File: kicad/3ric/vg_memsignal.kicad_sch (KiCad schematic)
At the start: 3 parts

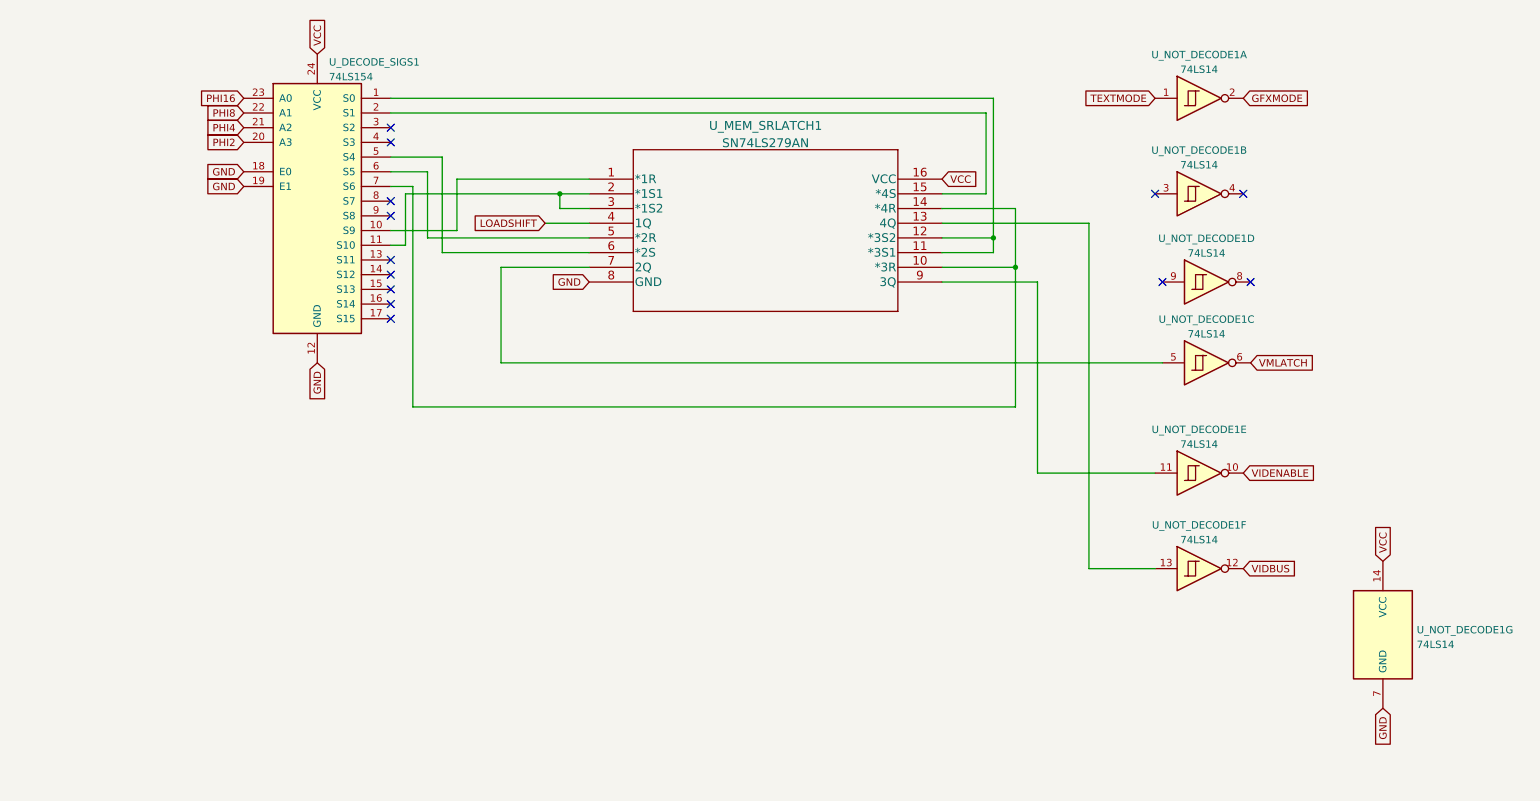
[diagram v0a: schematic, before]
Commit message: schematic updates - bring the schematics up to match breadboard changes current state has high res Apple II color emulation working
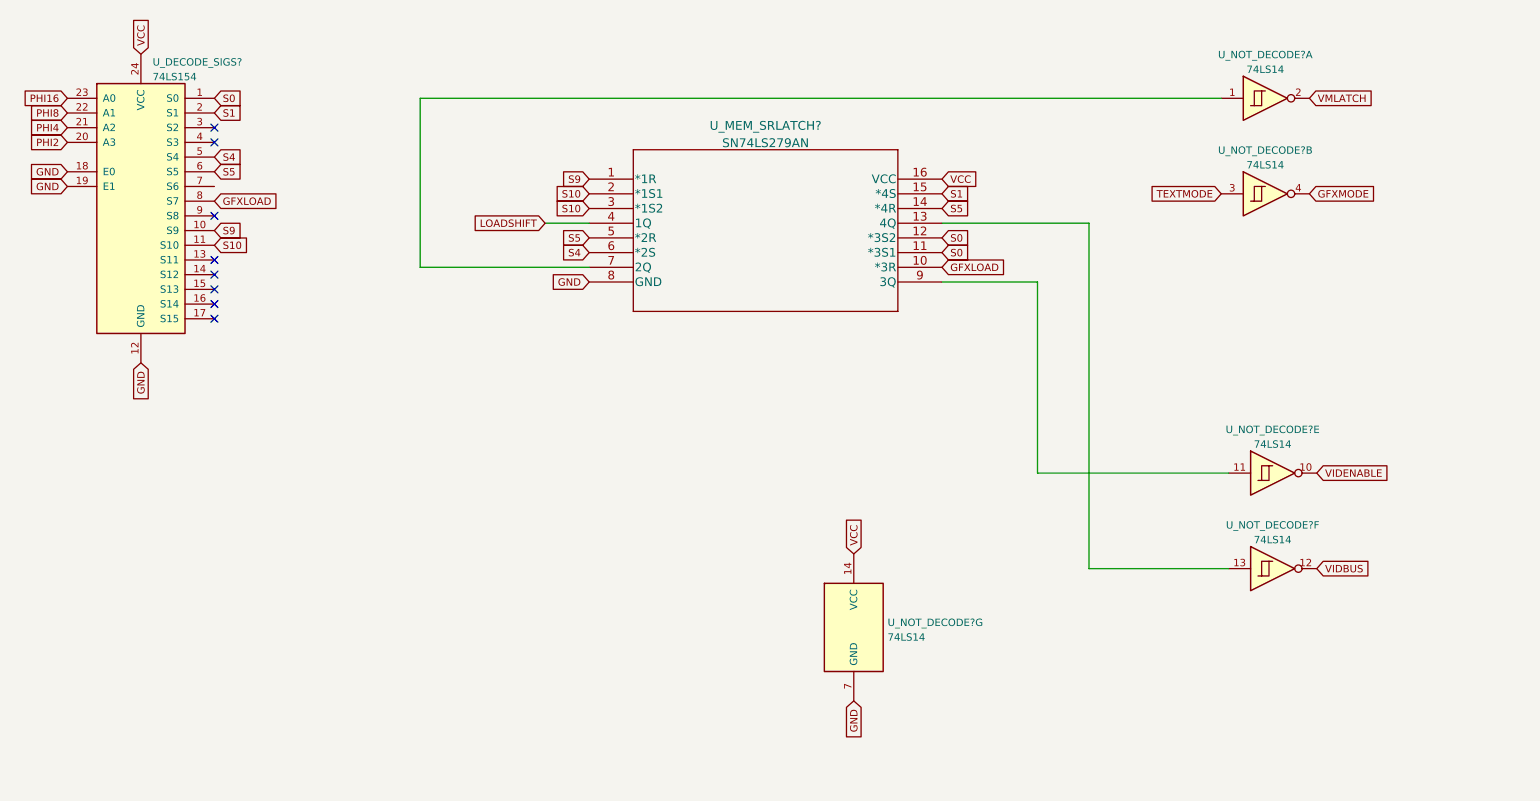
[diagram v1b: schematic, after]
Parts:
- removed unit 4 of U_NOT_DECODE1
- removed unit 3 of U_NOT_DECODE1
- renumbered U_DECODE_SIGS1 to U_DECODE_SIGS?, U_MEM_SRLATCH1 to U_MEM_SRLATCH?, U_NOT_DECODE1 to U_NOT_DECODE?
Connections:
- net GFXMODE: now also U_NOT_DECODE?.4; no longer U_NOT_DECODE?.2
- net TEXTMODE: now also U_NOT_DECODE?.3; no longer U_NOT_DECODE?.1
- net VMLATCH: now also U_NOT_DECODE?.2
- net at U_MEM_SRLATCH?.7 (2Q): now also U_NOT_DECODE?.1
- net S0: now reaches U_DECODE_SIGS?.1 (S0), U_MEM_SRLATCH?.11 (*3S1), U_MEM_SRLATCH?.12 (*3S2)
- net S9: now reaches U_DECODE_SIGS?.10 (S9), U_MEM_SRLATCH?.1 (*1R)
- net S10: now reaches U_DECODE_SIGS?.11 (S10), U_MEM_SRLATCH?.2 (*1S1), U_MEM_SRLATCH?.3 (*1S2)
- net S1: now reaches U_DECODE_SIGS?.2 (S1), U_MEM_SRLATCH?.15 (*4S)
- net S4: now reaches U_DECODE_SIGS?.5 (S4), U_MEM_SRLATCH?.6 (*2S)
- net S5: now reaches U_DECODE_SIGS?.6 (S5), U_MEM_SRLATCH?.5 (*2R)
- net S5: now also U_MEM_SRLATCH?.14 (*4R)
- net GFXLOAD: now reaches U_DECODE_SIGS?.8 (S7)
- net GFXLOAD: now also U_MEM_SRLATCH?.10 (*3R)
- now unconnected: U_DECODE_SIGS?.7 (S6)
- no-connect marks 13 -> 8
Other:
- moved on the sheet: U_DECODE_SIGS?, U_NOT_DECODE?A, U_NOT_DECODE?B, U_NOT_DECODE?E, U_NOT_DECODE?F, U_NOT_DECODE?G

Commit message: updates to logisim project and schematics
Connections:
- net GFXMODE: no longer names the net of U_NOT_DECODE?.4
- net TEXTMODE: no longer names the net of U_NOT_DECODE?.3
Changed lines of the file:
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@@
-    )
-  )
-  (global_label "GFXMODE" (shape input) (at 238.76 60.96 0) (fields_autoplaced)
-    (effects (font (size 1.27 1.27)) (justify left))
-    (property "Intersheet References" "${INTERSHEET_REFS}" (id 0) (at 249.9421 60.8806 0)
-      (effects (font (size 1.27 1.27)) (justify left) hide)
     )
   )
@@
     )
   )
-  (global_label "TEXTMODE" (shape input) (at 223.52 60.96 180) (fields_autoplaced)
-    (effects (font (size 1.27 1.27)) (justify right))
-    (property "Intersheet References" "${INTERSHEET_REFS}" (id 0) (at 211.6121 61.0394 0)
-      (effects (font (size 1.27 1.27)) (justify right) hide)
-    )
-  )

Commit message: push schematic updates
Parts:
- removed U_NOT_DECODE?: 74LS14, Package_DIP:DIP-14_W7.62mm_Socket, symbol 74xx:74LS14
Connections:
- net S9 is gone; now on net GFXLOAD: U_DECODE_SIGS?.10 (S9), U_MEM_SRLATCH?.1 (*1R)
- net GFXLOAD: no longer U_DECODE_SIGS?.8 (S7)
- net S4: no longer U_MEM_SRLATCH?.6 (*2S)
- net S5: no longer U_DECODE_SIGS?.6 (S5), U_MEM_SRLATCH?.5 (*2R)
- net !VIDENABLE: now reaches U_MEM_SRLATCH?.9 (3Q), U_NOT_DECODE?.11
- net at U_NOT_DECODE?.1: no longer U_MEM_SRLATCH?.7 (2Q)
- net VMLATCH: no longer names the net of U_NOT_DECODE?.2
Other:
- note added: "todo: update from breadboard"
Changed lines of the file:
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@@
 (kicad_sch (version 20211123) (generator eeschema)
   (paper "A4")
+  (junction (at 205.74 109.22) (diameter 0) (color 0 0 0 0)
+  )
+  (junction (at 57.15 67.31) (diameter 0) (color 0 0 0 0)
+  )
   (no_connect (at 49.53 82.55))
   (no_connect (at 49.53 52.07))
@@
   (no_connect (at 49.53 49.53))
   (no_connect (at 49.53 64.77))
-  (wire (pts (xy 191.77 109.22) (xy 224.79 109.22))
+  (wire (pts (xy 191.77 109.22) (xy 205.74 109.22))
     (stroke (width 0) (type default) (color 0 0 0 0))
   )
@@
     (stroke (width 0) (type default) (color 0 0 0 0))
   )
+  (wire (pts (xy 57.15 63.5) (xy 57.15 67.31))
+    (stroke (width 0) (type default) (color 0 0 0 0))
+  )
   (wire (pts (xy 200.66 66.04) (xy 200.66 125.73))
     (stroke (width 0) (type default) (color 0 0 0 0))
@@
     (stroke (width 0) (type default) (color 0 0 0 0))
   )
-  (wire (pts (xy 223.52 44.45) (xy 85.09 44.45))
+  (wire (pts (xy 209.55 104.14) (xy 205.74 104.14))
+    (stroke (width 0) (type default) (color 0 0 0 0))
+  )
+  (wire (pts (xy 57.15 67.31) (xy 49.53 67.31))
+    (stroke (width 0) (type default) (color 0 0 0 0))
+  )
+  (wire (pts (xy 205.74 109.22) (xy 224.79 109.22))
     (stroke (width 0) (type default) (color 0 0 0 0))
   )
@@
     (stroke (width 0) (type default) (color 0 0 0 0))
   )
-  (wire (pts (xy 85.09 73.66) (xy 114.3 73.66))
+  (wire (pts (xy 60.96 63.5) (xy 57.15 63.5))
+    (stroke (width 0) (type default) (color 0 0 0 0))
+  )
+  (wire (pts (xy 67.31 67.31) (xy 57.15 67.31))
+    (stroke (width 0) (type default) (color 0 0 0 0))
+  )
+  (wire (pts (xy 205.74 104.14) (xy 205.74 109.22))
     (stroke (width 0) (type default) (color 0 0 0 0))
   )
@@
     (stroke (width 0) (type default) (color 0 0 0 0))
   )
-  (wire (pts (xy 85.09 44.45) (xy 85.09 73.66))
-    (stroke (width 0) (type default) (color 0 0 0 0))
-  )
   (wire (pts (xy 191.77 76.2) (xy 191.77 109.22))
     (stroke (width 0) (type default) (color 0 0 0 0))
   )
+  (text "todo: update from breadboard\n" (at 67.31 90.17 0)
+    (effects (font (size 1.27 1.27)) (justify left bottom))
+  )
   (global_label "S4" (shape input) (at 49.53 54.61 0) (fields_autoplaced)
     (effects (font (size 1.27 1.27)) (justify left))
@@
     )
   )
-  (global_label "VMLATCH" (shape input) (at 238.76 44.45 0) (fields_autoplaced)
-    (effects (font (size 1.27 1.27)) (justify left))
-    (property "Intersheet References" "${INTERSHEET_REFS}" (id 0) (at 249.3979 44.3706 0)
-      (effects (font (size 1.27 1.27)) (justify left) hide)
-    )
-  )
   (global_label "PHI4" (shape input) (at 24.13 49.53 180) (fields_autoplaced)
     (effects (font (size 1.27 1.27)) (justify right))
@@
     )
   )
-  (global_label "GND" (shape input) (at 160.02 148.59 270) (fields_autoplaced)
-    (effects (font (size 1.27 1.27)) (justify right))
-    (property "Intersheet References" "${INTERSHEET_REFS}" (id 0) (at 159.9406 154.8736 90)
-      (effects (font (size 1.27 1.27)) (justify right) hide)
-    )
-  )
-  (global_label "VCC" (shape input) (at 160.02 123.19 90) (fields_autoplaced)
-    (effects (font (size 1.27 1.27)) (justify left))
-    (property "Intersheet References" "${INTERSHEET_REFS}" (id 0) (at 159.9406 117.1483 90)
-      (effects (font (size 1.27 1.27)) (justify left) hide)
-    )
-  )
   (global_label "S0" (shape input) (at 175.26 71.12 0) (fields_autoplaced)
     (effects (font (size 1.27 1.27)) (justify left))
@@
     )
   )
-  (global_label "S4" (shape input) (at 114.3 71.12 180) (fields_autoplaced)
-    (effects (font (size 1.27 1.27)) (justify right))
-    (property "Intersheet References" "${INTERSHEET_REFS}" (id 0) (at 109.4679 71.1994 0)
-      (effects (font (size 1.27 1.27)) (justify right) hide)
-    )
-  )
   (global_label "S0" (shape input) (at 49.53 44.45 0) (fields_autoplaced)
     (effects (font (size 1.27 1.27)) (justify left))
@@
     )
   )
+  (global_label "!VIDENABLE" (shape input) (at 209.55 104.14 0) (fields_autoplaced)
+    (effects (font (size 1.27 1.27)) (justify left))
+    (property "Intersheet References" "${INTERSHEET_REFS}" (id 0) (at 222.5464 104.0606 0)
+      (effects (font (size 1.27 1.27)) (justify left) hide)
+    )
+  )
   (global_label "GFXLOAD" (shape input) (at 175.26 73.66 0) (fields_autoplaced)
     (effects (font (size 1.27 1.27)) (justify left))
@@
     )
   )
-  (global_label "S5" (shape input) (at 49.53 57.15 0) (fields_autoplaced)
-    (effects (font (size 1.27 1.27)) (justify left))
-    (property "Intersheet References" "${INTERSHEET_REFS}" (id 0) (at 54.3621 57.0706 0)
-      (effects (font (size 1.27 1.27)) (justify left) hide)
-    )
-  )
   (global_label "S5" (shape input) (at 175.26 63.5 0) (fields_autoplaced)
     (effects (font (size 1.27 1.27)) (justify left))
@@
     )
   )
-  (global_label "S9" (shape input) (at 49.53 67.31 0) (fields_autoplaced)
-    (effects (font (size 1.27 1.27)) (justify left))
-    (property "Intersheet References" "${INTERSHEET_REFS}" (id 0) (at 54.3621 67.2306 0)
-      (effects (font (size 1.27 1.27)) (justify left) hide)
-    )
-  )
-  (global_label "GFXLOAD" (shape input) (at 49.53 62.23 0) (fields_autoplaced)
-    (effects (font (size 1.27 1.27)) (justify left))
-    (property "Intersheet References" "${INTERSHEET_REFS}" (id 0) (at 60.2283 62.1506 0)
+  (global_label "S9" (shape input) (at 67.31 67.31 0) (fields_autoplaced)
+    (effects (font (size 1.27 1.27)) (justify left))
+    (property "Intersheet References" "${INTERSHEET_REFS}" (id 0) (at 72.1421 67.2306 0)
       (effects (font (size 1.27 1.27)) (justify left) hide)
     )
@@
     )
   )
-  (global_label "S5" (shape input) (at 114.3 68.58 180) (fields_autoplaced)
-    (effects (font (size 1.27 1.27)) (justify right))
-    (property "Intersheet References" "${INTERSHEET_REFS}" (id 0) (at 109.4679 68.6594 0)
-      (effects (font (size 1.27 1.27)) (justify right) hide)
-    )
-  )
   (global_label "PHI2" (shape input) (at 24.13 52.07 180) (fields_autoplaced)
     (effects (font (size 1.27 1.27)) (justify right))
@@
     (property "Intersheet References" "${INTERSHEET_REFS}" (id 0) (at 17.8464 57.0706 0)
       (effects (font (size 1.27 1.27)) (justify right) hide)
+    )
+  )
+  (global_label "GFXLOAD" (shape input) (at 60.96 63.5 0) (fields_autoplaced)
+    (effects (font (size 1.27 1.27)) (justify left))
+    (property "Intersheet References" "${INTERSHEET_REFS}" (id 0) (at 71.6583 63.4206 0)
+      (effects (font (size 1.27 1.27)) (justify left) hide)
     )
   )
@@
       (effects (font (size 1.27 1.27)) hide)
     )
-    (pin "1")
-    (pin "2")
-    (pin "3")
-    (pin "4")
-    (pin "5")
-    (pin "6")
-    (pin "8")
-    (pin "9")
-    (pin "10")
-    (pin "11")
-    (pin "12")
-    (pin "13")
-    (pin "14")
-    (pin "7")
-  )
-  (symbol (lib_id "74xx:74LS14") (at 160.02 135.89 0) (unit 7)
-    (in_bom yes) (on_board yes) (fields_autoplaced)
-    (property "Reference" "U_NOT_DECODE?" (id 0) (at 165.862 135.0553 0)
-      (effects (font (size 1.27 1.27)) (justify left))
-    )
-    (property "Value" "74LS14" (id 1) (at 165.862 137.5922 0)
-      (effects (font (size 1.27 1.27)) (justify left))
-    )
-    (property "Footprint" "Package_DIP:DIP-14_W7.62mm_Socket" (id 2) (at 160.02 135.89 0)
-      (effects (font (size 1.27 1.27)) hide)
-    )
-    (property "Datasheet" "http://www.ti.com/lit/gpn/sn74LS14" (id 3) (at 160.02 135.89 0)
-      (effects (font (size 1.27 1.27)) hide)
-    )

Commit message: update schematics
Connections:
- net !VIDENABLE: now also U_NOT_DECODE?.1
- net GFXLOAD: now also U_NOT_DECODE?.4; no longer U_DECODE_SIGS?.10 (S9), U_MEM_SRLATCH?.1 (*1R), U_MEM_SRLATCH?.10 (*3R)
- net S0: now also U_NOT_DECODE?.3
- net S4: now also U_MEM_SRLATCH?.14 (*4R)
- net S5: now also U_DECODE_SIGS?.6 (S5), U_MEM_SRLATCH?.10 (*3R); no longer U_MEM_SRLATCH?.14 (*4R)
- net S11: now reaches U_DECODE_SIGS?.13 (S11)
- net S11: now also U_MEM_SRLATCH?.5 (*2R)
- net S13: now reaches U_DECODE_SIGS?.15 (S13)
- net S13: now also U_MEM_SRLATCH?.6 (*2S)
- net VIDENABLE2: now reaches U_NOT_DECODE?.2
- net SS_WRITE_SIGNAL: now reaches U_MEM_SRLATCH?.7 (2Q)
- new net S9: U_DECODE_SIGS?.10 (S9), U_MEM_SRLATCH?.1 (*1R)
- no-connect marks 8 -> 6
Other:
- moved on the sheet: U_NOT_DECODE?A, U_NOT_DECODE?B
